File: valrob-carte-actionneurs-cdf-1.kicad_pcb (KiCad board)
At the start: 4 copper layers, 138 parts, among them J1 USB_C_Receptacle_USB2.0_14P, J2 Conn_01x02, J3 Conn_01x02, J4 Conn_01x04_Pin, J5 Conn_01x02, J6 Conn_01x02, M1 Motor_Servo, M10 Motor_Servo, M11 Motor_Servo, M12 Motor_Servo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

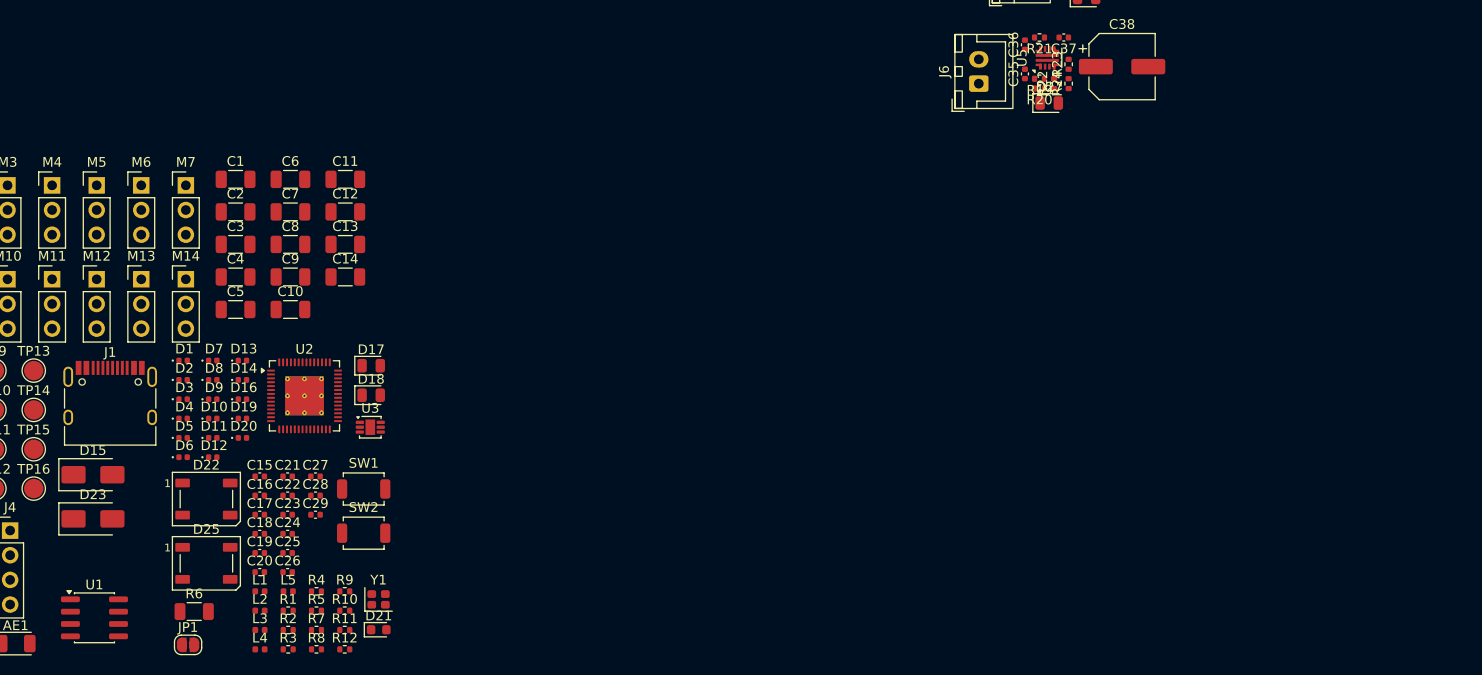
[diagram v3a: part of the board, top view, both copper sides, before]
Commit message: pcb: add USB C initial layout
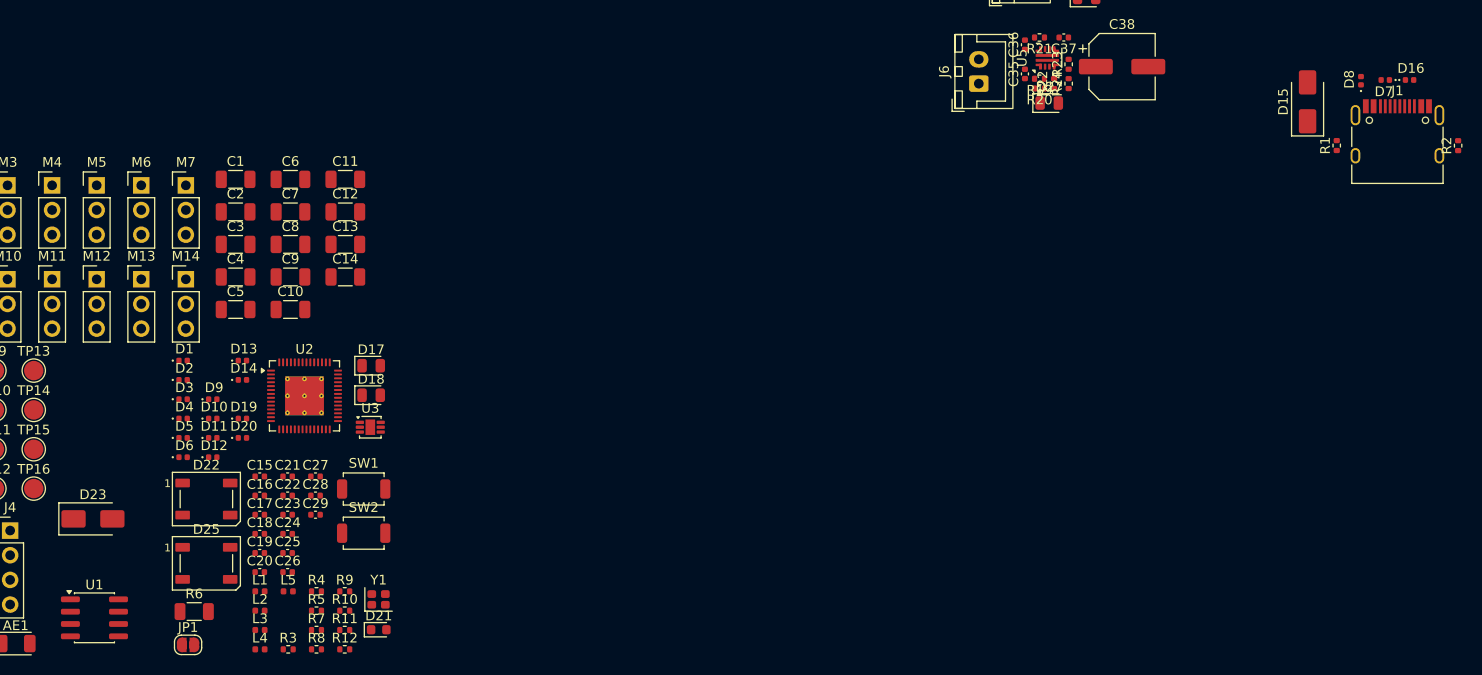
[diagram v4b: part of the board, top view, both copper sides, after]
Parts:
- moved J1 135.2 mm to (180.2, 113.8)
- moved D15 130.8 mm to (171.0, 109.2), turned to 90 degrees
- moved R2 130.4 mm to (186.5, 113.8), turned to 90 degrees
- moved D16 124.6 mm to (181.5, 107.0)
- moved D7 124.1 mm to (179.0, 107.0), turned to 180 degrees
- moved D8 122.2 mm to (176.5, 107.1), turned to 90 degrees
- moved R1 118.1 mm to (174.0, 113.8), turned to 90 degrees

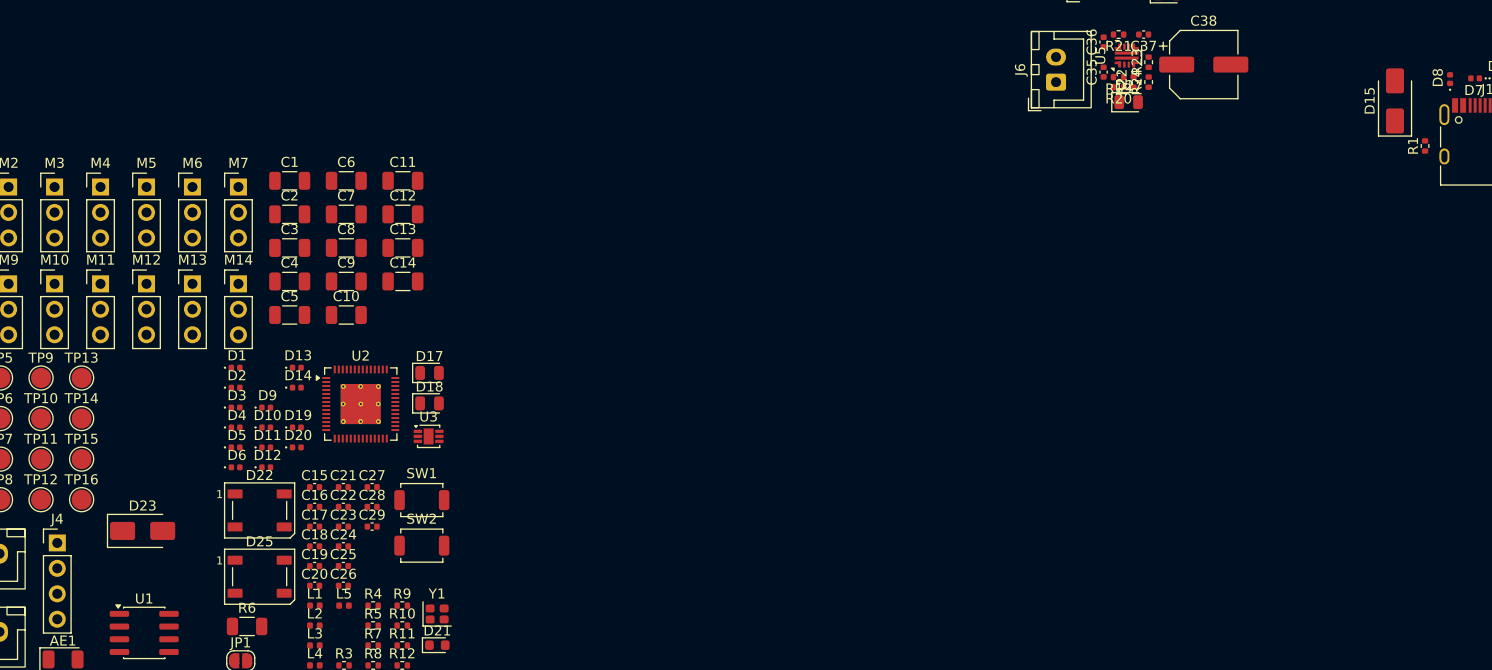
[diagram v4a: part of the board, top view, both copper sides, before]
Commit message: pcb: add LDL212 3V3 ldo initial layout
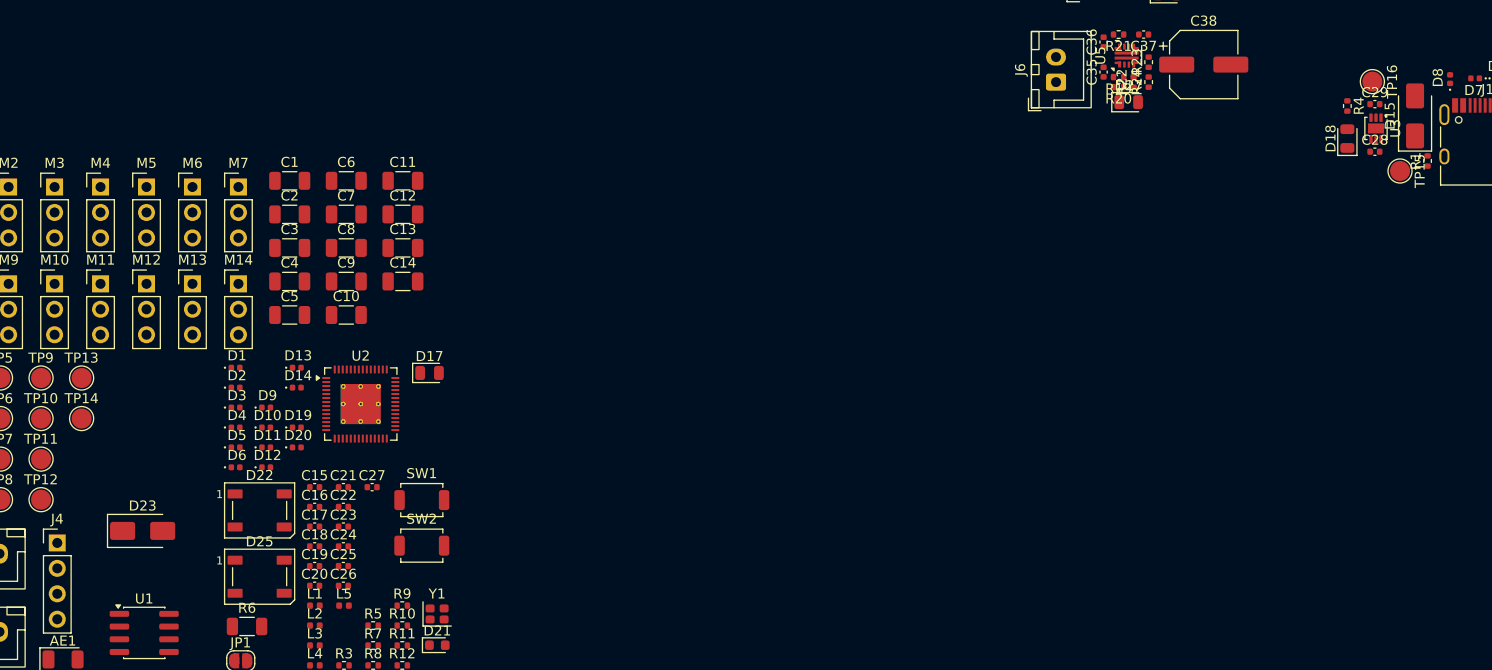
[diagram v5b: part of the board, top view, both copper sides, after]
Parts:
- moved TP16 135.5 mm to (168.7, 107.3), turned to -90 degrees
- moved TP15 134.8 mm to (171.5, 116.2), turned to -90 degrees
- moved R4 109.3 mm to (166.2, 109.8), turned to -90 degrees
- moved C29 108.7 mm to (169.0, 109.6)
- moved C28 106.2 mm to (169.0, 114.3)
- moved U3 99.5 mm to (169.1, 112.0), turned to -90 degrees
- moved D18 95.4 mm to (166.2, 113.0), turned to 90 degrees
- moved D15 2.50 mm to (173.0, 110.8)
- moved R1 1.52 mm to (174.2, 115.2)

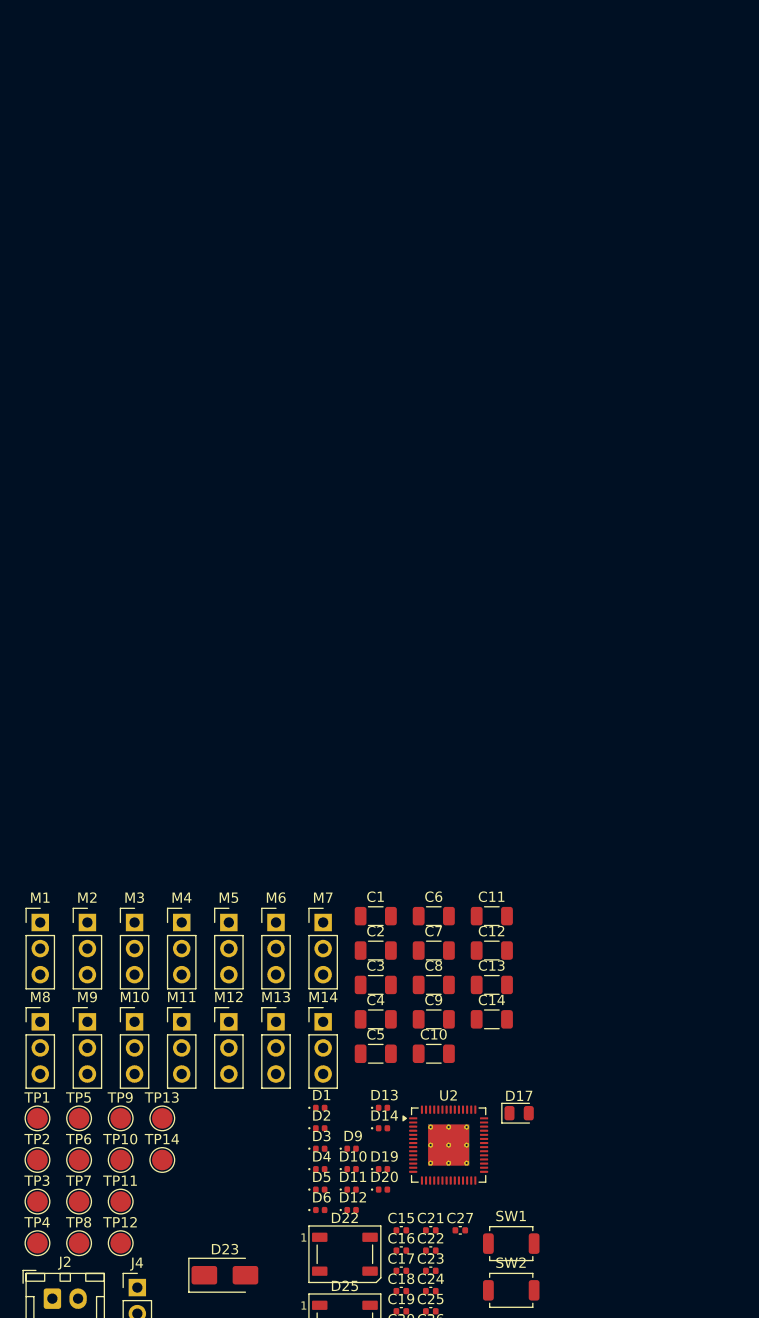
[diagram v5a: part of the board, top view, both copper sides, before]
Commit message: pcb: initial servo routing
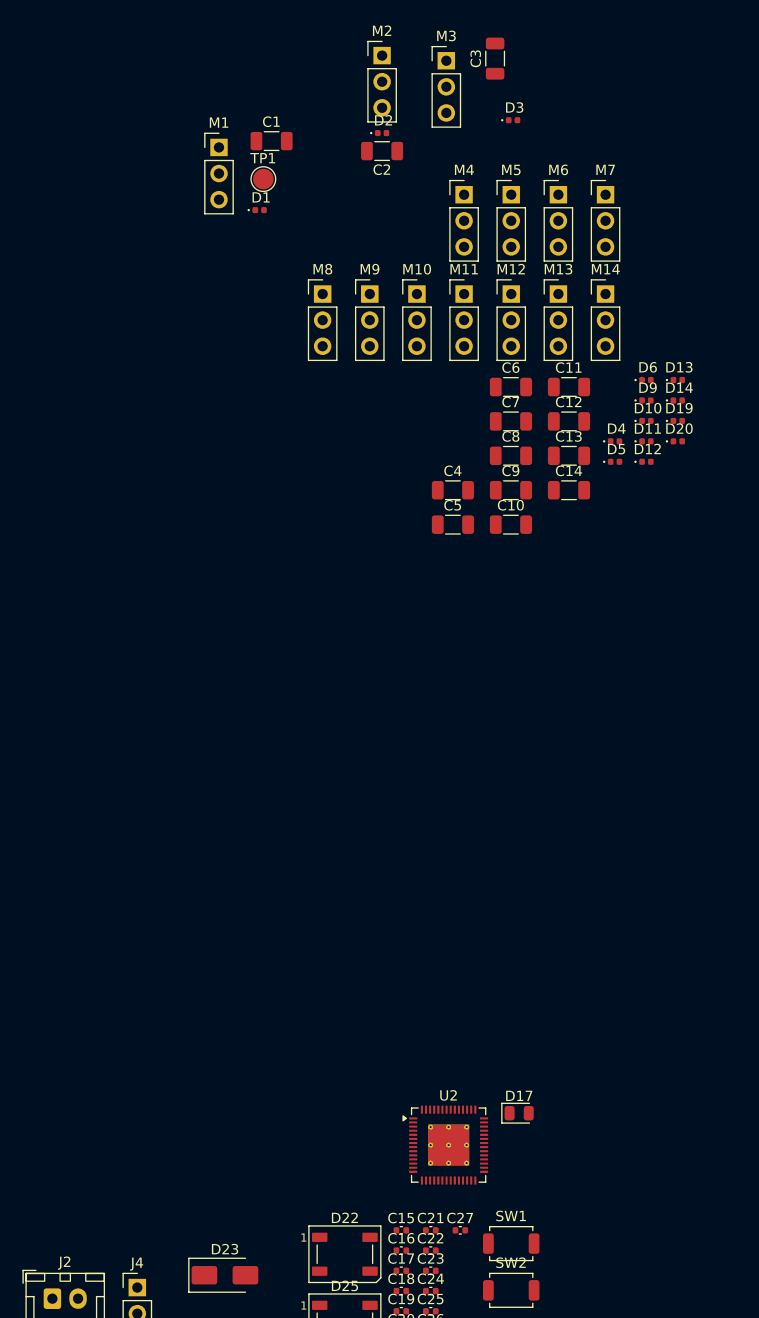
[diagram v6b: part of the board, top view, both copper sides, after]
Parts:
- removed TP10, TP11, TP12, TP13, TP14, TP2, TP3, TP4, TP5, TP6, TP7, TP8, TP9: TestPoint, TestPoint:TestPoint_Pad_D2.0mm
- moved D3 101.9 mm to (74.0, 39.8)
- moved D2 97.1 mm to (61.2, 41.0)
- moved TP1 94.0 mm to (49.7, 45.5)
- moved C3 90.9 mm to (72.2, 33.8), turned to 90 degrees
- moved M3 89.2 mm to (67.5, 34.0)
- moved M2 89.1 mm to (61.2, 33.5)
- moved D1 87.6 mm to (49.3, 48.5)
- moved D6 86.8 mm to (87.0, 65.0)
- moved D10 78.3 mm to (87.0, 69.0)
- moved D19 78.3 mm to (90.0, 69.0)
- moved D11 78.3 mm to (87.0, 71.0)
- moved D12 78.3 mm to (87.0, 73.0)
- moved D9 78.3 mm to (87.0, 67.0)
- moved D20 78.3 mm to (90.0, 71.0)
- moved C2 77.8 mm to (61.2, 42.8), turned to 180 degrees
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
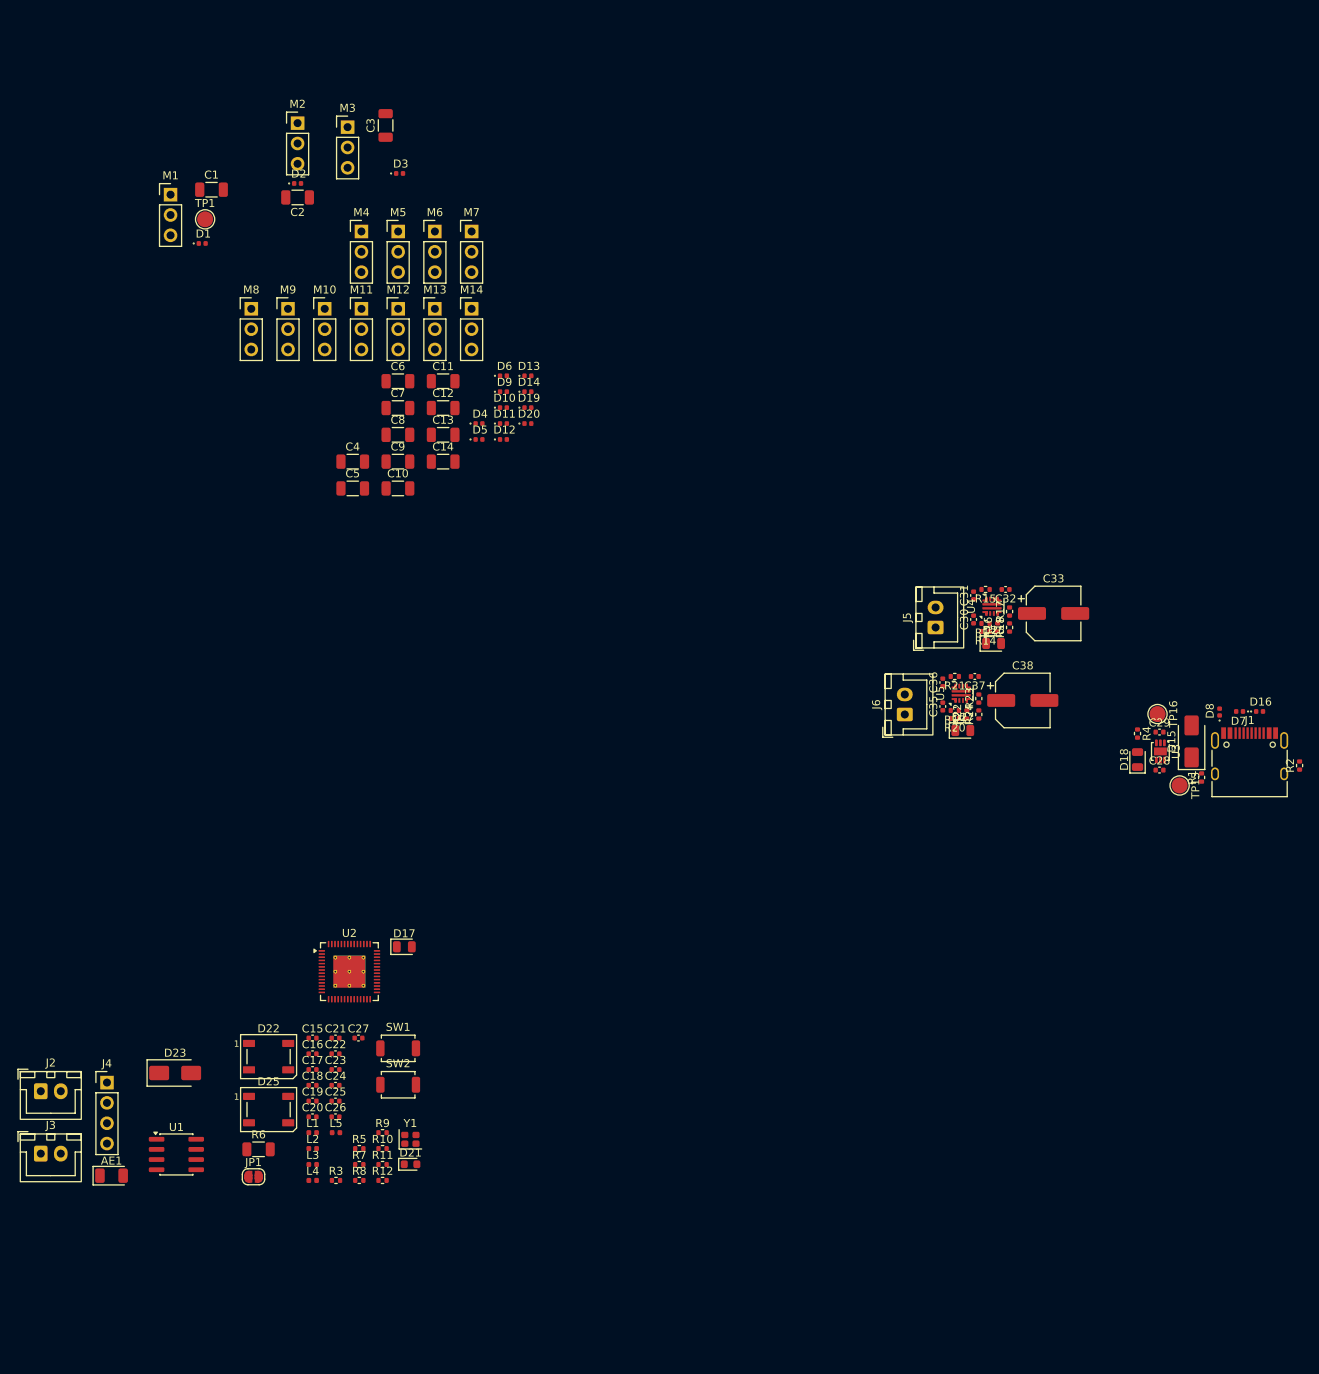
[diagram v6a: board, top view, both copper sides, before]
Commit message: schem: add servo initial layout
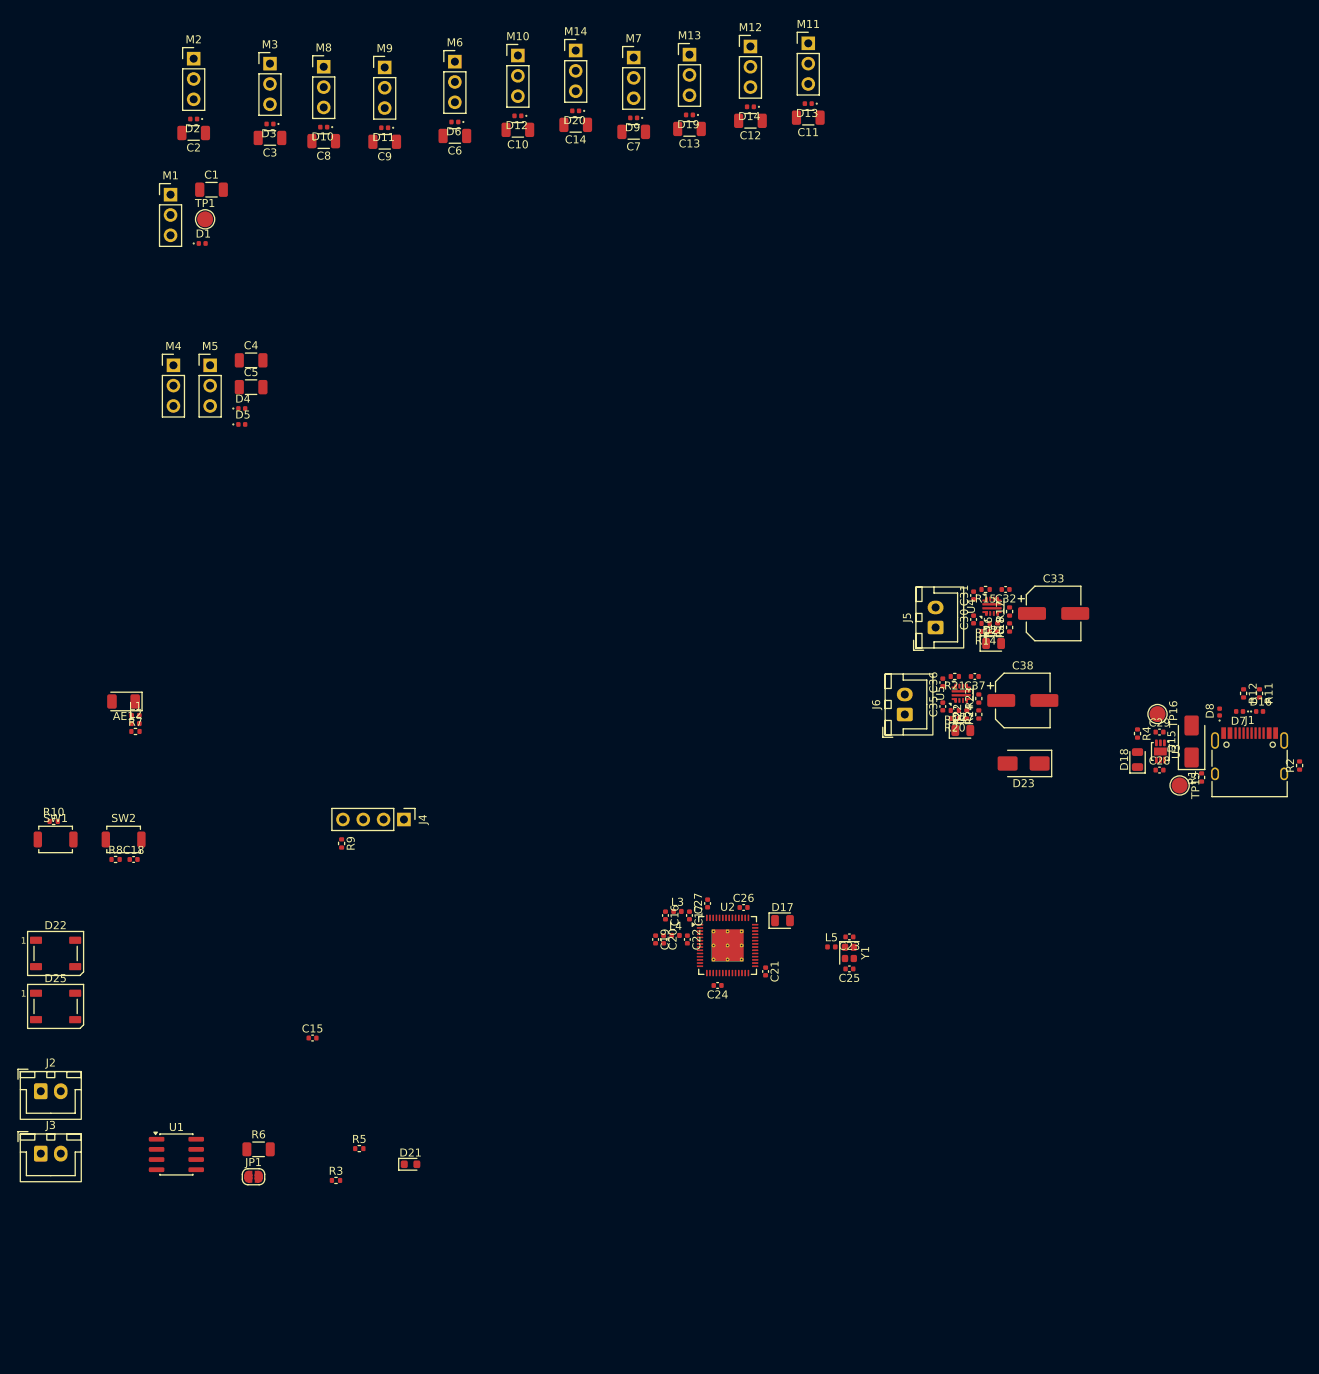
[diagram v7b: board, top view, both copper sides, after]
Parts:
- moved R11 124.4 mm to (181.5, 104.7), turned to -90 degrees
- moved R12 123.7 mm to (179.5, 104.7), turned to -90 degrees
- moved D23 112.9 mm to (152.0, 113.5), turned to 180 degrees
- moved C23 66.3 mm to (130.2, 135.2), turned to 180 degrees
- moved C25 66.3 mm to (130.2, 139.2), turned to 180 degrees
- moved L5 66.1 mm to (128.0, 136.4)
- moved M11 65.0 mm to (125.1, 23.5)
- moved R7 60.9 mm to (41.0, 109.5)
- moved Y1 59.6 mm to (130.2, 137.2), turned to -90 degrees
- moved AE1 59.3 mm to (39.5, 105.8), turned to 180 degrees
- moved R10 58.0 mm to (30.8, 120.8)
- moved L2 57.6 mm to (41.0, 108.5)
- moved C26 57.3 mm to (117.0, 131.5)
- moved L1 56.7 mm to (41.0, 107.5)
- moved C11 56.3 mm to (125.1, 32.8), turned to 180 degrees
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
